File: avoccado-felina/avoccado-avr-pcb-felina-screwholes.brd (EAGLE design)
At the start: 42.5 x 17.5 mm, 81 parts, among them Q1 16MHz, Q2 FET, U1 MPU-6000QFN-24, U2 MCP73831

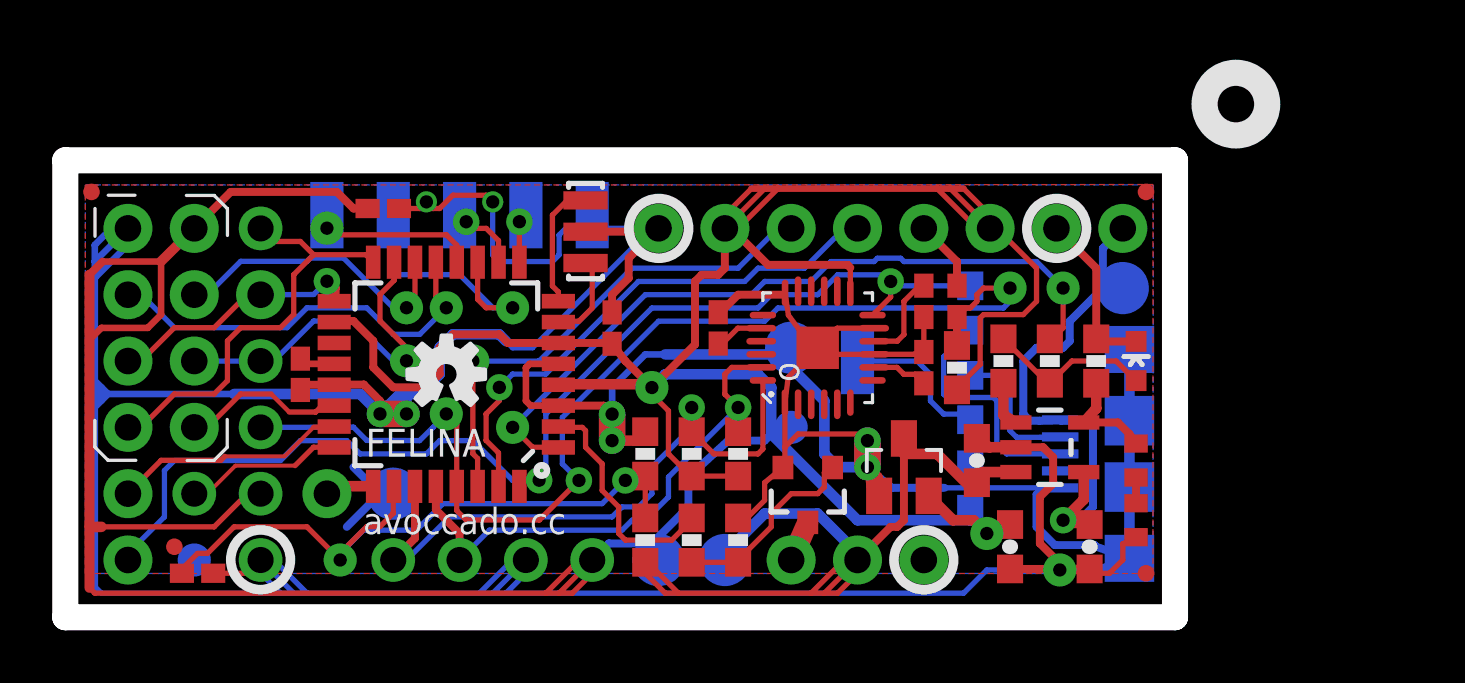
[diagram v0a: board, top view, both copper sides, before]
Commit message: add Felina fork with screw holes
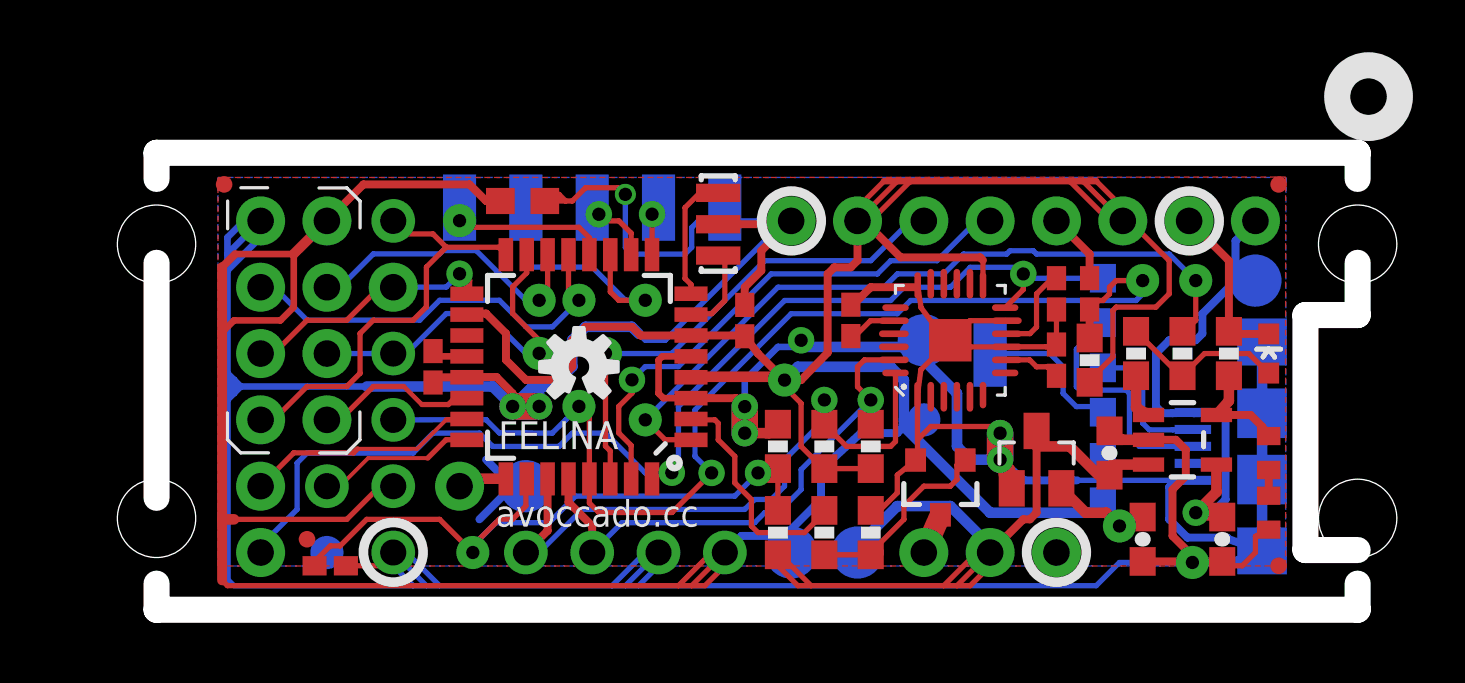
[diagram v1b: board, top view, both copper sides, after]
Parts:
- C10: device rcl:C0402K -> rcl:C0603
- moved C10 5.34 mm to (17.0, 15.7)
- moved C11 5.09 mm to (37.5, 9.56)
- moved C6 5.09 mm to (40.8, 2.70)
- moved C8 5.09 mm to (37.5, 12.1)
- moved D1 5.09 mm to (45.6, 9.81)
- moved JP10 5.09 mm to (37.5, 14.9)
- moved JP18 5.09 mm to (40.0, 14.9)
- moved JP25 5.09 mm to (37.5, 2.19)
- moved R12 5.09 mm to (45.6, 6.00)
- moved R13 5.09 mm to (39.2, 11.8)
- moved R14 5.09 mm to (39.2, 8.41)
- moved R15 5.09 mm to (39.2, 4.99)
- moved R3 5.09 mm to (44.1, 9.81)
- moved R9 5.09 mm to (45.6, 3.72)
- moved C3 5.09 mm to (25.5, 11.1)
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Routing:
- net GND: track 227.8 -> 227.3 mm
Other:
- board size 42.5 x 17.5 mm -> 46 x 17.5 mm
- board text added: "VB"
- board text removed: "o"

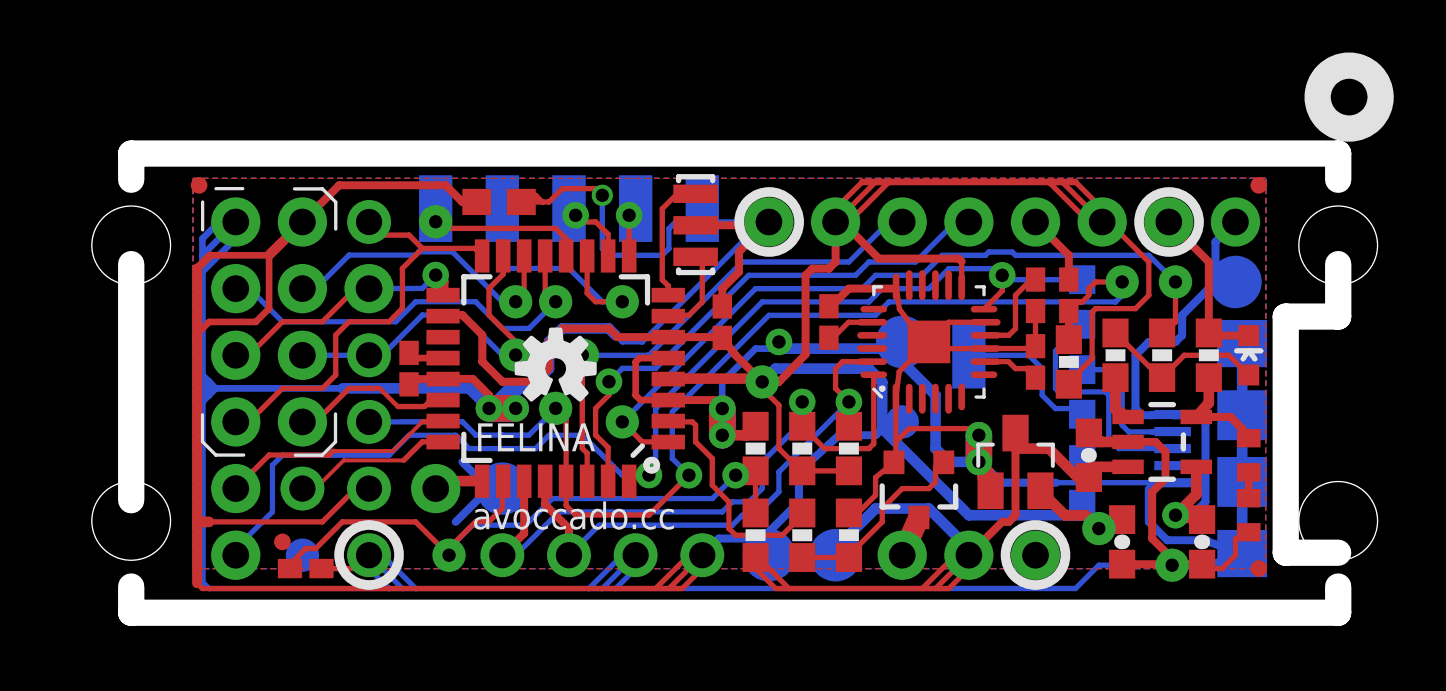
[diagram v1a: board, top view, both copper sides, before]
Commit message: daisy chainable tab layout
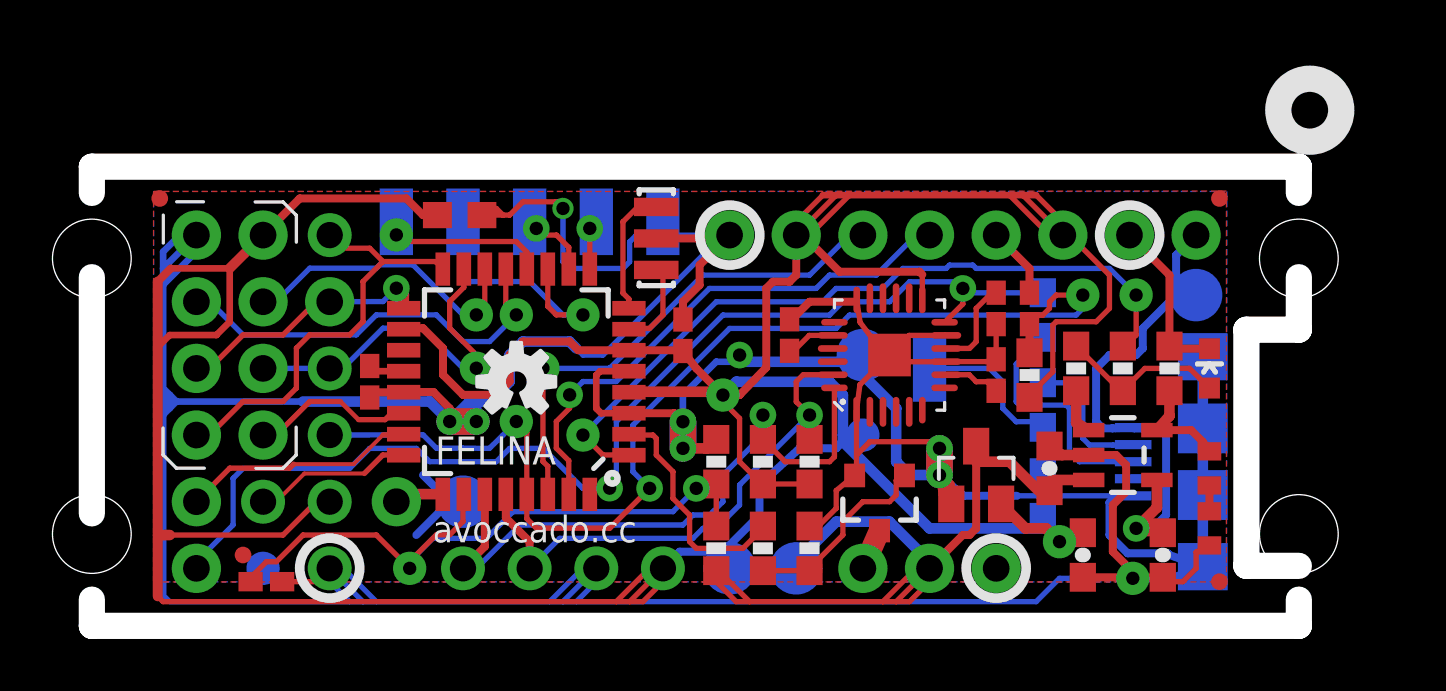
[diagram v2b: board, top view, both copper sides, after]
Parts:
- moved Q2 1.58 mm to (31.5, 4.23)
- moved U1 1.58 mm to (31.9, 9.82)
- moved FID1 1.58 mm to (4.09, 15.8)
- moved FID2 1.58 mm to (44.5, 15.8)
- moved C1 1.58 mm to (12.1, 8.80)
- moved C10 1.58 mm to (15.5, 15.2)
- moved C11 1.58 mm to (36.0, 9.06)
- moved C2 1.58 mm to (37.2, 11.6)
- moved C3 1.58 mm to (24.0, 10.6)
- moved C4 1.58 mm to (42.3, 2.20)
- moved C5 1.58 mm to (38.0, 5.50)
- moved C6 1.58 mm to (39.3, 2.20)
- moved C7 1.58 mm to (8.15, 1.18)
- moved C8 1.58 mm to (36.0, 11.6)
- moved C9 1.58 mm to (28.1, 10.6)
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
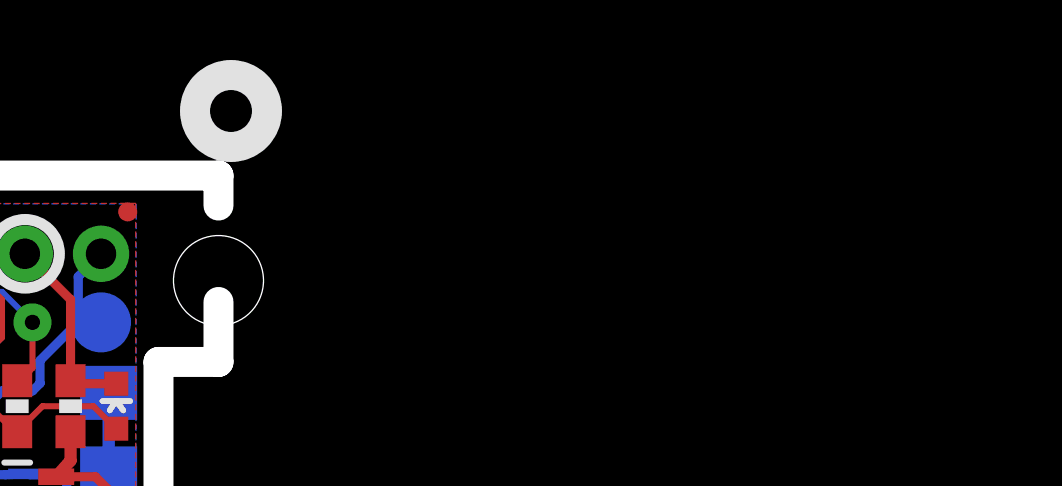
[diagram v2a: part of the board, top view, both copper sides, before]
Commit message: render schematic PNG
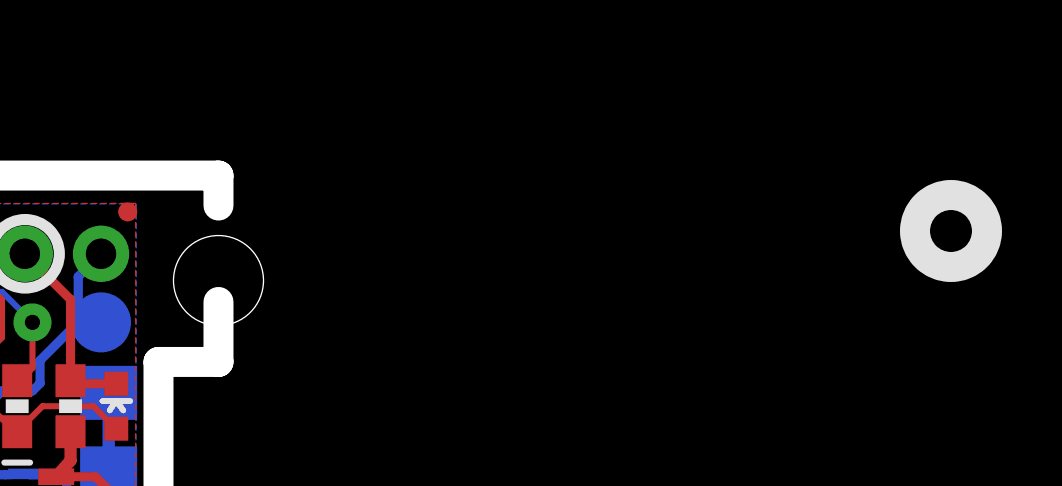
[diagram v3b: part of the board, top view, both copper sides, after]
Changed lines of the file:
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@@
 <text x="14.591" y="6.718" size="1.0668" layer="21" ratio="15" align="top-left">FELINA</text>
 <text x="14.491146875" y="3.6990625" size="1.016" layer="21" ratio="15" rot="SR0" align="top-left">avoccado.cc</text>
-<circle x="47.917" y="19.152" radius="1.2" width="1" layer="21"/>
+<circle x="71.917" y="15.152" radius="1.2" width="1" layer="21"/>
 <wire x1="1.5" y1="12.787" x2="1.5" y2="3.787" width="1" layer="46"/>
 <wire x1="1.5" y1="0.5" x2="1.5" y2="-0.5" width="1" layer="46"/>

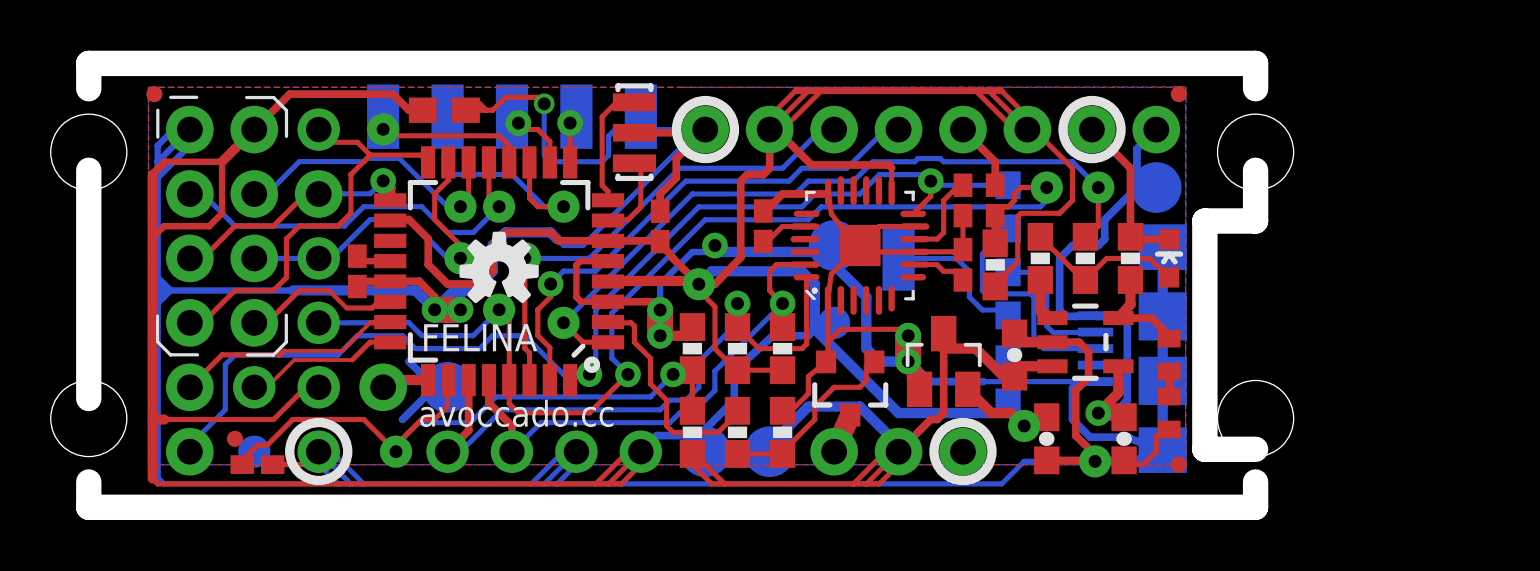
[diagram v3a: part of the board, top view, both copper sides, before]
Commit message: ditch right mounting holes, rearrange USB
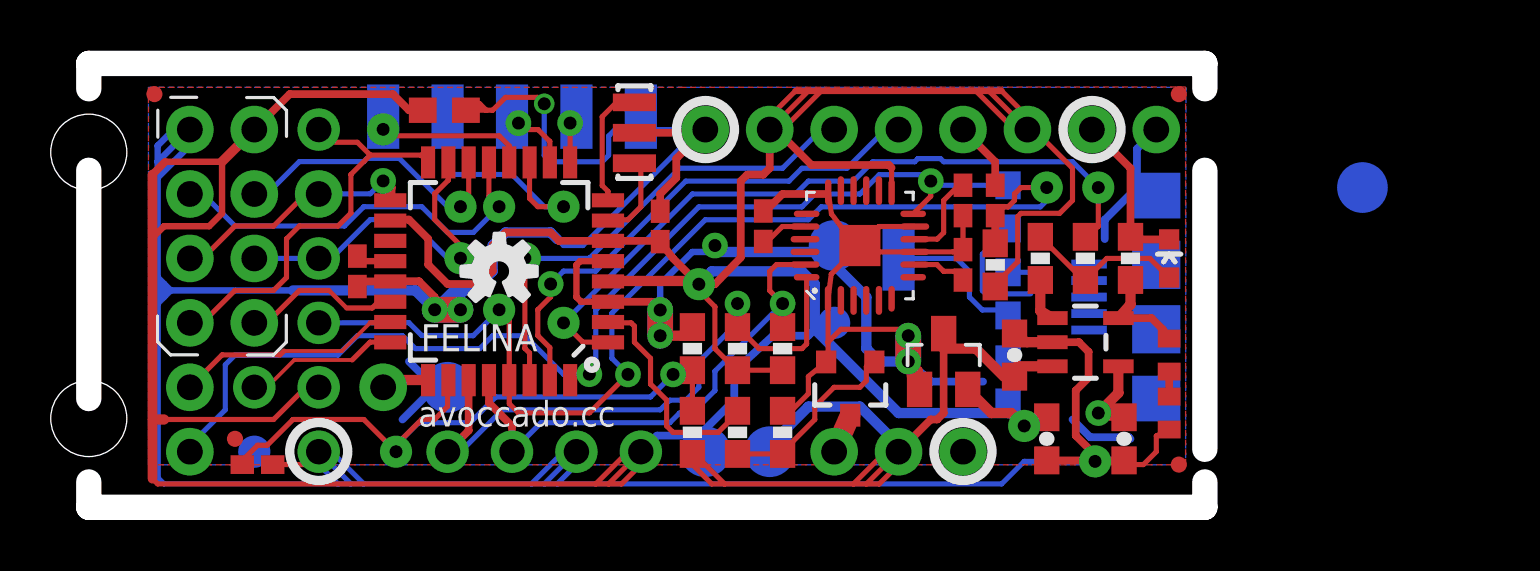
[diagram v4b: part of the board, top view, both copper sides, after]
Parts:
- moved TP14 8.13 mm to (51.7, 12.1)
- moved JP7 2.05 mm to (43.6, 7.79)
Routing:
- net GND: track 227.3 -> 210.6 mm
- net 5V: track 20.9 -> 8.73 mm
- net N$4: track 9.25 -> 4.83 mm
- net N$5: track 5.40 -> 1.05 mm
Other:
- board size 46 x 17.5 mm -> 44 x 17.5 mm

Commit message: new footprint for USB
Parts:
- removed JP7: USB-MICROB, SparkFun-Connectors:USB-MICROB
- added JP22: USB_MICROB_PLUGCONN-11752, SparkFun-Connectors:USB-B-MICRO-SMD_V03
- moved TP14 4.89 mm to (52.5, 16.9)
- moved R6 3.13 mm to (43.9, 9.31), turned to 90 degrees
- moved D1 2.68 mm to (43.8, 12.0)
- moved JP17 2.54 mm to (41.0, 14.4)
- moved JP6 2.54 mm to (43.6, 14.4)
- moved R3 0.38 mm to (42.2, 9.31)
- moved R12 0.13 mm to (44.0, 5.50)
- moved R9 0.13 mm to (44.0, 3.22)
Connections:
- net 5V: now also JP22.VBUS1; no longer JP7.VBUS
- net GND: now also JP22.GND1, JP22.SHIELD1, JP22.SHIELD2, JP22.SHIELD3; no longer JP7.GND, JP7.MT1, JP7.MT2
- net N$4: now also JP22.D+1; no longer JP7.D+
- net N$5: now also JP22.D-1; no longer JP7.D-
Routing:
- net GND: track 210.6 -> 218.8 mm
- net LED: track 6.45 -> 1.10 mm
- net D3: track 28.6 -> 31.9 mm
- net N$5: track 1.05 -> 2.60 mm
- net N$4: track 4.83 -> 6.09 mm

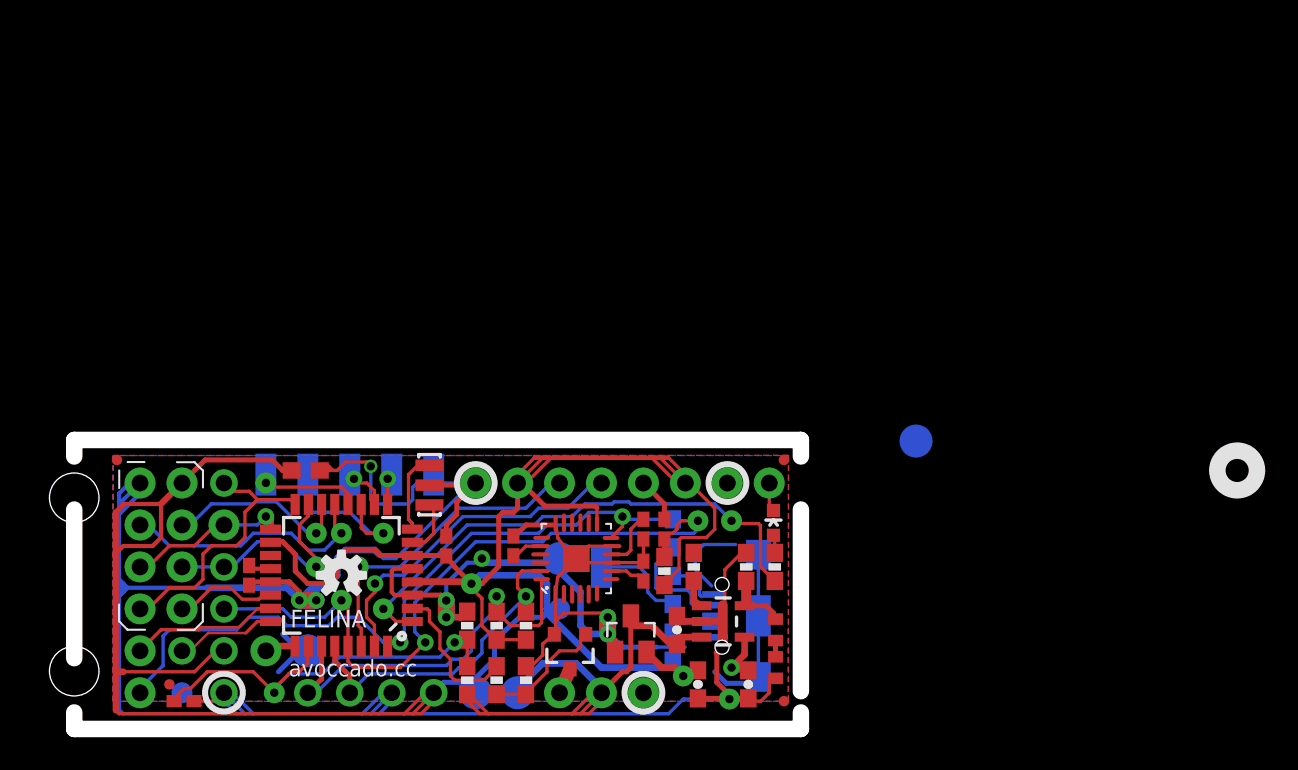
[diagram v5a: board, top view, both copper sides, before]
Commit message: eliminated redundant 0402 Rs for Rp
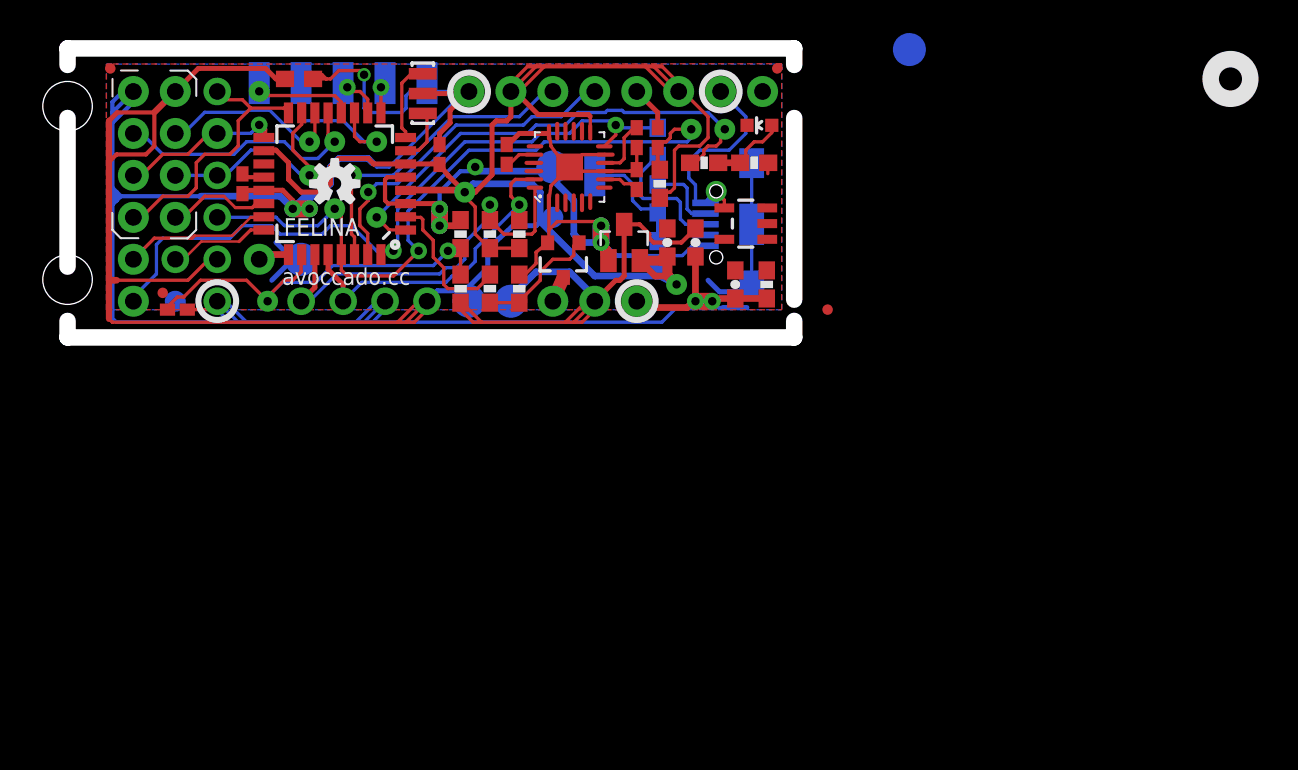
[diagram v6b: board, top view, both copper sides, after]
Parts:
- removed R12, R9: 1K, rcl:R0402
- moved C6 26.8 mm to (37.4, 29.0), turned to 90 degrees
- moved R6 24.8 mm to (39.6, 33.8), turned to 0 degrees
- moved R4 24.7 mm to (42.7, 33.8), turned to 0 degrees
- moved C4 24.2 mm to (41.5, 26.4)
- moved U2 24.1 mm to (42.2, 30.1), turned to 90 degrees
- moved D1 24.1 mm to (43.0, 36.1), turned to 90 degrees
- moved FID4 23.9 mm to (47.1, 24.9)
- moved R14 23.7 mm to (36.8, 31.6)
- moved R13 23.7 mm to (36.8, 35.1)
- moved R15 23.7 mm to (36.8, 28.2)
- moved JP14 23.7 mm to (10.2, 33.0)
- moved JP28 23.7 mm to (5.08, 33.0)
- moved TP11 23.7 mm to (33.0, 33.0)
- moved C10 23.7 mm to (15.1, 38.9)
- moved FID3 23.7 mm to (6.86, 25.9)
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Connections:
- removed net N$3: R12.1, R9.2
- net CHG-PROG: no longer R12.2
- net GND: no longer R9.1
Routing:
- net GND: track 218.8 -> 211.1 mm, vias 9 -> 10
- net 5V: track 8.50 -> 12.8 mm
- net CHG-PROG: track 3.86 -> 0.00 mm
- net LED: track 1.10 -> 4.69 mm
- net 3.3V: track 164.0 -> 166.9 mm
- net D3: track 31.9 -> 29.7 mm
- net N$4: track 6.09 -> 8.08 mm
- net N$5: track 2.60 -> 4.37 mm
- net SOC: track 1.77 -> 0.66 mm
- net N$3: track 0.99 -> 0.00 mm
- net 7-TO-D-: track 7.57 -> 7.06 mm
- net D2-INT: track 43.6 -> 43.1 mm
